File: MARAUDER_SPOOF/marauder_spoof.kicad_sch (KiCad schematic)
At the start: 26 parts, among them J2 Conn_01x10_Socket, J2 GPS, J3 Coil, J3 Conn_01x08_Socket, J4 Conn_01x08_Socket, J5 Conn_01x10_Socket, P1 USB_C_Plug_USB2.0, Q1 DMP2004TK-7, Q2 DMP2004TK-7, SW7 RESET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

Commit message: update layout magspoof-wifi
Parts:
- removed F1: 0.5A, Fuse:Fuse_0805_2012Metric, symbol Device:Fuse_Small
- removed J4: Conn_01x08_Socket, Connector_PinHeader_2.54mm:PinHeader_1x08_P2.54mm_Vertical, symbol Connector:Conn_01x08_Socket
- removed J5: Conn_01x10_Socket, Connector_PinHeader_2.54mm:PinHeader_1x10_P2.54mm_Vertical, symbol Connector:Conn_01x10_Socket
- removed Q1, Q2: DMP2004TK-7, Package_TO_SOT_THT:TO-92_Inline, symbol Transistor_FET:BS250
- added C4: 10uF, Capacitor_SMD:C_0603_1608Metric, symbol Device:C_Small
- added Q1, Q2: DMP2004TK-7, Package_TO_SOT_SMD:SOT-23, symbol Device:Q_NMOS_GSD
- J2: footprint Connector_PinHeader_2.54mm:PinHeader_1x10_P2.54mm_Horizontal -> Connector_PinHeader_2.54mm:PinHeader_1x10_P2.54mm_Vertical
- J3: footprint Connector_PinHeader_2.54mm:PinHeader_1x08_P2.54mm_Horizontal -> Connector_PinHeader_2.54mm:PinHeader_1x08_P2.54mm_Vertical
- R5, R6, R7, R8, R9: footprint (none) -> Resistor_SMD:R_0603_1608Metric
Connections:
- net +3V3: now also C4.1
- net GND: now also C4.2
- net at R8.1: now also Q1.2 (S)
- net at R6.1, R7.2: now also Q1.1 (G), Q2.1 (G)
- net at R6.2: now also Q1.3 (D), Q2.3 (D)
- net at R9.1: now also Q2.2 (S)
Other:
- moved on the sheet: C4

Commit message: Add_resistors_BOM_
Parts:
- P1: LCSC# C2987386 -> C2760486
- Q1, Q2: manf# (none) -> DMP2004TK-7; provedor (none) -> MOUSER
- R5, R6: LCSC# (none) -> C217281; manf# (none) -> CR-03JL7---10K; provedor (none) -> LCSC
- R7: LCSC# (none) -> C2692872; provedor (none) -> LCSC
- R8, R9: LCSC# (none) -> C394547; provedor (none) -> LCSC
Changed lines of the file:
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@@
+      (effects (font (size 1.27 1.27)) hide)
+    )
+    (property "LCSC#" "C394547" (at 202.184 139.446 0)
+      (effects (font (size 1.27 1.27)) hide)
+    )
+    (property "provedor" "LCSC" (at 202.184 139.446 0)
       (effects (font (size 1.27 1.27)) hide)
     )
@@
       (effects (font (size 1.27 1.27)) hide)
     )
+    (property "manf#" "DMP2004TK-7" (at 212.344 129.54 0)
+      (effects (font (size 1.27 1.27)) hide)
+    )
+    (property "provedor" "MOUSER" (at 212.344 129.54 0)
+      (effects (font (size 1.27 1.27)) hide)
+    )
     (pin "1")
     (pin "2")
@@
     )
     (property "Datasheet" "~" (at 191.008 113.919 0)
+      (effects (font (size 1.27 1.27)) hide)
+    )
+    (property "LCSC#" "C217281" (at 191.008 113.919 0)
+      (effects (font (size 1.27 1.27)) hide)
+    )
+    (property "manf#" "CR-03JL7---10K" (at 191.008 113.919 0)
+      (effects (font (size 1.27 1.27)) hide)
+    )
+    (property "provedor" "LCSC" (at 191.008 113.919 0)
       (effects (font (size 1.27 1.27)) hide)
     )
@@
       (effects (font (size 1.27 1.27)) hide)
     )
-    (property "LCSC#" "C2987386" (at 113.284 133.731 0)
+    (property "LCSC#" "C2760486" (at 113.284 133.731 0)
       (effects (font (size 1.27 1.27)) hide)
     )
@@
       (effects (font (size 1.27 1.27)) hide)
     )
+    (property "LCSC#" "C2692872" (at 181.356 120.269 0)
+      (effects (font (size 1.27 1.27)) hide)
+    )
+    (property "provedor" "LCSC" (at 181.356 120.269 0)
+      (effects (font (size 1.27 1.27)) hide)
+    )
     (pin "1")
     (pin "2")
@@
       (effects (font (size 1.27 1.27)) hide)
     )
+    (property "LCSC#" "C394547" (at 214.884 139.446 0)
+      (effects (font (size 1.27 1.27)) hide)
+    )
+    (property "provedor" "LCSC" (at 214.884 139.446 0)
+      (effects (font (size 1.27 1.27)) hide)
+    )
     (pin "1")
     (pin "2")
@@
       (effects (font (size 1.27 1.27)) hide)
     )
+    (property "manf#" "DMP2004TK-7" (at 199.644 120.269 0)
+      (effects (font (size 1.27 1.27)) hide)
+    )
+    (property "provedor" "MOUSER" (at 199.644 120.269 0)
+      (effects (font (size 1.27 1.27)) hide)
+    )
     (pin "1")
     (pin "2")
@@
       (effects (font (size 1.27 1.27)) hide)
     )
+    (property "LCSC#" "C217281" (at 177.038 52.324 0)
+      (effects (font (size 1.27 1.27)) hide)
+    )
+    (property "manf#" "CR-03JL7---10K" (at 177.038 52.324 0)
+      (effects (font (size 1.27 1.27)) hide)
+    )
+    (property "provedor" "LCSC" (at 177.038 52.324 0)
+      (effects (font (size 1.27 1.27)) hide)
+    )

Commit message: Add_subg_BOM
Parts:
- Q1, Q2: footprint Package_TO_SOT_SMD:SOT-23 -> Package_TO_SOT_SMD:SOT-523
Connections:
- no-connect marks 19 -> 29
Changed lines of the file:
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@@
   (junction (at 137.922 126.111) (diameter 0) (color 0 0 0 0)
   )
+  (no_connect (at 182.372 73.914))
   (no_connect (at 228.6 73.914))
   (no_connect (at 228.6 51.054))
   (no_connect (at 228.6 61.214))
+  (no_connect (at 182.245 43.434))
+  (no_connect (at 182.245 48.514))
   (no_connect (at 228.6 81.534))
+  (no_connect (at 233.68 86.614))
   (no_connect (at 53.213 37.973))
   (no_connect (at 228.6 63.754))
@@
   (no_connect (at 187.96 51.054))
   (no_connect (at 228.6 53.594))
+  (no_connect (at 182.245 81.534))
   (no_connect (at 228.6 78.994))
   (no_connect (at 27.813 37.973))
+  (no_connect (at 231.648 84.074))
   (no_connect (at 228.6 58.674))
   (no_connect (at 187.96 56.134))
+  (no_connect (at 182.245 76.454))
   (no_connect (at 228.6 76.454))
   (no_connect (at 228.6 68.834))
+  (no_connect (at 182.245 45.974))
   (no_connect (at 187.96 53.594))
   (no_connect (at 228.6 56.134))
+  (no_connect (at 182.245 84.074))
+  (no_connect (at 182.245 78.994))
   (polyline (pts (xy 13.4112 97.4344) (xy 285.5722 97.4344))
     (stroke (width 0) (type default))
@@
   )
   (wire (pts (xy 177.038 61.214) (xy 187.96 61.214))
-    (stroke (width 0) (type default))
-  )
-  (polyline (pts (xy 208.28 90.17) (xy 208.28 89.916))
     (stroke (width 0) (type default))
   )
@@
       (effects (font (size 1.27 1.27)) (justify left))
     )
-    (property "Footprint" "Package_TO_SOT_SMD:SOT-23" (at 217.424 127 0)
+    (property "Footprint" "Package_TO_SOT_SMD:SOT-523" (at 217.424 127 0)
       (effects (font (size 1.27 1.27)) hide)
     )
@@
       (effects (font (size 1.27 1.27)) (justify left))
     )
-    (property "Footprint" "Package_TO_SOT_SMD:SOT-23" (at 204.724 117.729 0)
-      (effects (font (size 1.27 1.27)) hide)
-    )
+    (property "Footprint" "Package_TO_SOT_SMD:SOT-523" (at 204.724 117.729 0)
+      (effects (font (size 1.27 1.27)) hide)
+    )

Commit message: Update_BOM
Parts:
- J2: manf# PZ254R-11-10P -> (none)
- J3: manf# WMRR138F-0 -> WR301025-19M8-G
- J3: manf# PZ254-1-08-W-8.5 -> (none)
- P1: manf# TYPE-C-31-M-31 -> (none)
- R10, R11: manf# ERJ3RBD5101V -> (none)
- R12, R5, R6: manf# CR-03JL7---10K -> (none)
- U3: manf# TC4424AVOA713 -> (none)
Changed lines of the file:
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@@
       (effects (font (size 1.27 1.27)) hide)
     )
-    (property "manf#" "CR-03JL7---10K" (at 191.008 113.919 0)
+    (property "manf#" "" (at 191.008 113.919 0)
       (effects (font (size 1.27 1.27)) hide)
     )
@@
       (effects (font (size 1.27 1.27)) hide)
     )
-    (property "manf#" "CR-03JL7---10K" (at 56.261 136.398 0)
+    (property "manf#" "" (at 56.261 136.398 0)
       (effects (font (size 1.27 1.27)) hide)
     )
@@
       (effects (font (size 1.27 1.27)) hide)
     )
-    (property "manf#" "WMRR138F-0" (at -183.5658 139.1666 0)
+    (property "manf#" "WR301025-19M8-G" (at -183.5658 139.1666 0)
       (effects (font (size 1.27 1.27)) hide)
     )
@@
       (effects (font (size 1.27 1.27)) hide)
     )
-    (property "manf#" "PZ254-1-08-W-8.5" (at 116.713 36.068 0)
+    (property "manf#" "" (at 116.713 36.068 0)
       (effects (font (size 1.27 1.27)) hide)
     )
@@
       (effects (font (size 1.27 1.27)) hide)
     )
-    (property "manf#" "TYPE-C-31-M-31" (at 113.284 133.731 0)
+    (property "manf#" "" (at 113.284 133.731 0)
       (effects (font (size 1.27 1.27)) hide)
     )
@@
       (effects (font (size 1.27 1.27)) hide)
     )
-    (property "manf#" "ERJ3RBD5101V" (at 132.842 126.111 0)
+    (property "manf#" "" (at 132.842 126.111 0)
       (effects (font (size 1.27 1.27)) hide)
     )
@@
       (effects (font (size 1.27 1.27)) hide)
     )
-    (property "manf#" "ERJ3RBD5101V" (at 132.842 123.571 0)
+    (property "manf#" "" (at 132.842 123.571 0)
       (effects (font (size 1.27 1.27)) hide)
     )
@@
       (effects (font (size 1.27 1.27)) hide)
     )
-    (property "manf#" "CR-03JL7---10K" (at 55.118 116.967 0)
+    (property "manf#" "" (at 55.118 116.967 0)
       (effects (font (size 1.27 1.27)) hide)
     )
@@
       (effects (font (size 1.27 1.27)) hide)
     )
-    (property "manf#" "CR-03JL7---10K" (at 177.038 52.324 0)
+    (property "manf#" "" (at 177.038 52.324 0)
       (effects (font (size 1.27 1.27)) hide)
     )
@@
       (effects (font (size 1.27 1.27)) hide)
     )
-    (property "manf#" "PZ254R-11-10P" (at 117.602 73.2536 0)
+    (property "manf#" "" (at 117.602 73.2536 0)
       (effects (font (size 1.27 1.27)) hide)
     )
@@
       (effects (font (size 1.524 1.524)) hide)
     )
-    (property "manf#" "TC4424AVOA713" (at 40.513 44.323 0)
-      (effects (font (size 1.27 1.27)) hide)
-    )
+    (property "manf#" "" (at 40.513 44.323 0)
+      (effects (font (size 1.27 1.27)) hide)
+    )

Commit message: BOM updated
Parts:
- J2: now not fitted
- J2: LCSC# C492418 -> C57369
- J3: LCSC# C2894950 -> C492407
- R10, R11: LCSC# C191782 -> C156350
- R12, R5, R6: LCSC# C217281 -> C2930027
- SW7, SW8: LCSC# C2886897 -> (none); manf# (none) -> TL3342F450QG
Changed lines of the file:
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@@
       (effects (font (size 1.27 1.27)) hide)
     )
-    (property "manf#" "" (at 48.133 120.523 0)
-      (effects (font (size 1.27 1.27)) hide)
-    )
-    (property "LCSC#" "C2886897" (at 48.133 120.523 0)
+    (property "manf#" "TL3342F450QG" (at 48.133 120.523 0)
+      (effects (font (size 1.27 1.27)) hide)
+    )
+    (property "LCSC#" "" (at 48.133 120.523 0)
       (effects (font (size 1.27 1.27)) hide)
     )
@@
       (effects (font (size 1.27 1.27)) hide)
     )
-    (property "LCSC#" "C217281" (at 191.008 113.919 0)
+    (property "LCSC#" "C2930027" (at 191.008 113.919 0)
       (effects (font (size 1.27 1.27)) hide)
     )
@@
       (effects (font (size 1.27 1.27)) hide)
     )
-    (property "LCSC#" "C217281" (at 56.261 136.398 0)
+    (property "LCSC#" "C2930027" (at 56.261 136.398 0)
       (effects (font (size 1.27 1.27)) hide)
     )
@@
       (effects (font (size 1.27 1.27)) hide)
     )
-    (property "LCSC#" "C2894950" (at 116.713 36.068 0)
+    (property "LCSC#" "C492407" (at 116.713 36.068 0)
       (effects (font (size 1.27 1.27)) hide)
     )
@@
       (effects (font (size 1.27 1.27)) hide)
     )
-    (property "manf#" "" (at 49.657 141.605 0)
-      (effects (font (size 1.27 1.27)) hide)
-    )
-    (property "LCSC#" "C2886897" (at 49.657 141.605 0)
+    (property "manf#" "TL3342F450QG" (at 49.657 141.605 0)
+      (effects (font (size 1.27 1.27)) hide)
+    )
+    (property "LCSC#" "" (at 49.657 141.605 0)
       (effects (font (size 1.27 1.27)) hide)
     )
@@
   )
   (symbol (lib_id "Connector:Screw_Terminal_01x05") (at 275.209 124.587 0) (unit 1)
-    (in_bom yes) (on_board yes) (dnp no) (fields_autoplaced)
+    (in_bom yes) (on_board yes) (dnp yes) (fields_autoplaced)
     (property "Reference" "J2" (at 277.241 124.5869 0)
       (effects (font (size 1.27 1.27)) (justify left))
@@
       (effects (font (size 1.27 1.27)) hide)
     )
-    (property "LCSC#" "C191782" (at 132.842 126.111 0)
+    (property "LCSC#" "C156350" (at 132.842 126.111 0)
       (effects (font (size 1.27 1.27)) hide)
     )
@@
       (effects (font (size 1.27 1.27)) hide)
     )
-    (property "LCSC#" "C191782" (at 132.842 123.571 0)
+    (property "LCSC#" "C156350" (at 132.842 123.571 0)
       (effects (font (size 1.27 1.27)) hide)
     )
@@
       (effects (font (size 1.27 1.27)) hide)
     )
-    (property "LCSC#" "C217281" (at 55.118 116.967 0)
+    (property "LCSC#" "C2930027" (at 55.118 116.967 0)
       (effects (font (size 1.27 1.27)) hide)
     )
@@
       (effects (font (size 1.27 1.27)) hide)
     )
-    (property "LCSC#" "C217281" (at 177.038 52.324 0)
+    (property "LCSC#" "C2930027" (at 177.038 52.324 0)
       (effects (font (size 1.27 1.27)) hide)
     )
@@
       (effects (font (size 1.27 1.27)) hide)
     )
-    (property "LCSC#" "C492418" (at 117.602 73.2536 0)
-      (effects (font (size 1.27 1.27)) hide)
-    )
+    (property "LCSC#" "C57369" (at 117.602 73.2536 0)
+      (effects (font (size 1.27 1.27)) hide)
+    )

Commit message: MarauderSpoof's BOM updated
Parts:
- U1: value ESP32-S3-WROOM-1U-N16 -> ESP32-S3-WROOM-1U-N4; manf# ESP32-S3-WROOM-1U-N16 -> ESP32-S3-WROOM-1U-N4
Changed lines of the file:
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@@
       (effects (font (size 1.524 1.524)))
     )
-    (property "Value" "ESP32-S3-WROOM-1U-N16" (at 208.28 28.194 0)
+    (property "Value" "ESP32-S3-WROOM-1U-N4" (at 208.28 28.194 0)
       (effects (font (size 1.524 1.524)))
     )
@@
       (effects (font (size 1.524 1.524)) hide)
     )
-    (property "manf#" "ESP32-S3-WROOM-1U-N16" (at 187.96 35.814 0)
+    (property "manf#" "ESP32-S3-WROOM-1U-N4" (at 187.96 35.814 0)
       (effects (font (size 1.27 1.27)) hide)
     )

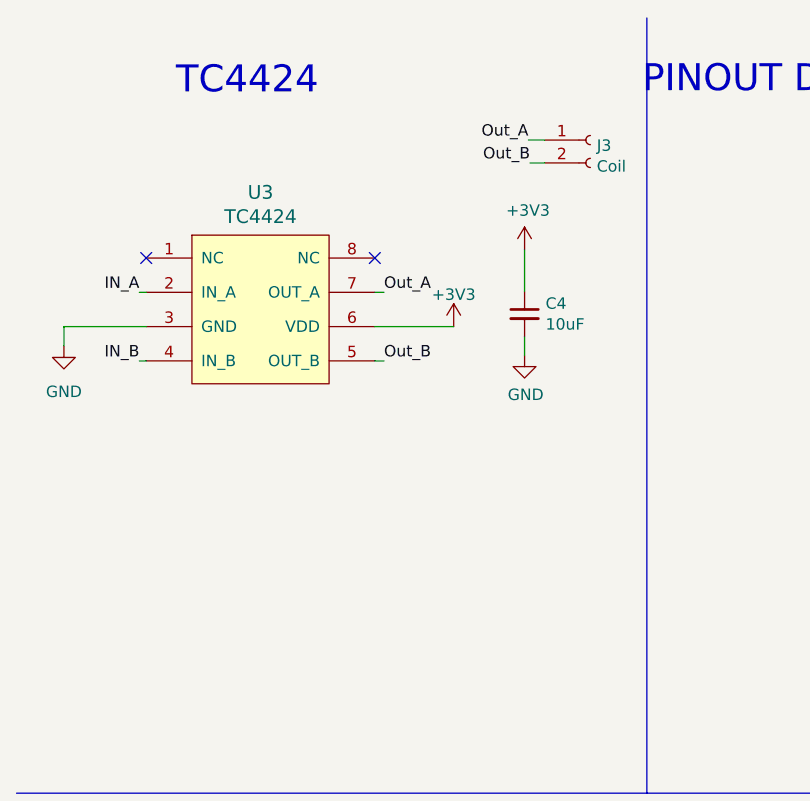
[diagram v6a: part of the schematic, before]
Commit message: feat(hw):Update coil
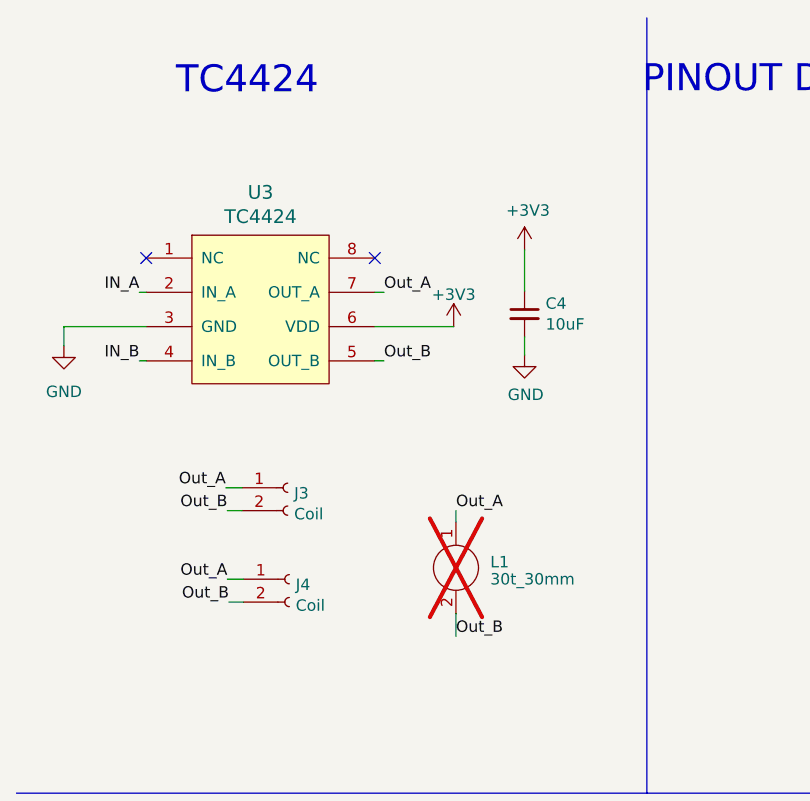
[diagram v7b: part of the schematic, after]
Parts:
- added J4: Coil, Connector_PinHeader_2.54mm:PinHeader_1x02_P2.54mm_Vertical, symbol Connector:Conn_01x02_Female
- added L1: 30t_30mm, Library:Coil_30t_30mm_0.2_0.2_0.6_0.3, symbol Magspoof:Coil_20t_35mm_0.2_0.6_0.3
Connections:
- net Out_A: now also J4.1 (Pin_1), L1.1
- net Out_B: now also J4.2 (Pin_2), L1.2
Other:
- moved on the sheet: J3

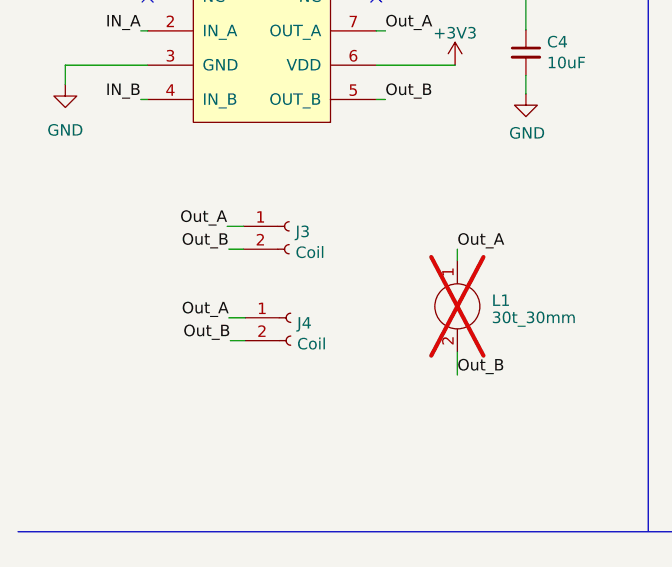
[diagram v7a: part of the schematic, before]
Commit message: fix(hw): add DNP for J1 and J4 and update SW1,2 and Q1,2 mfr.#
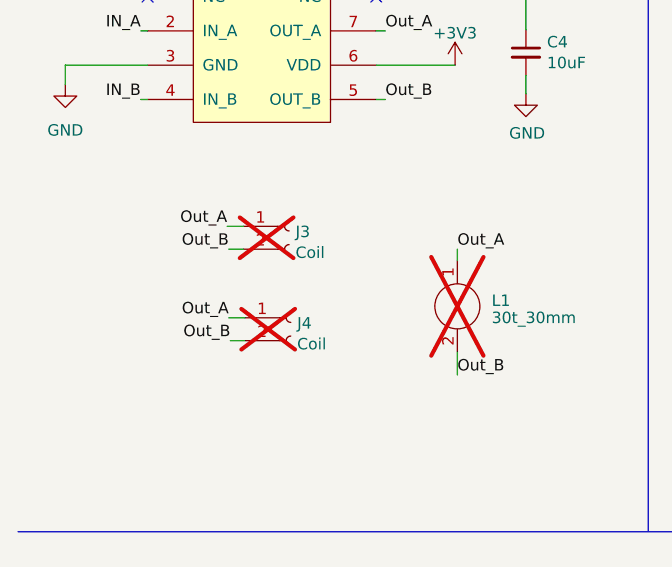
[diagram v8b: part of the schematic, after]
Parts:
- J3, J4: now not fitted
- Q1, Q2: LCSC# (none) -> C461051
- SW7: LCSC# (none) -> C318889
- SW8: LCSC# (none) -> C2886897
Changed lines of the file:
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@@
 			)
 		)
-		(property "LCSC#" ""
+		(property "LCSC#" "C318889 "
 			(at 48.133 120.523 0)
 			(effects
@@
 			)
 		)
+		(property "LCSC#" "C461051"
+			(at 212.344 129.54 0)
+			(effects
+				(font
+					(size 1.27 1.27)
+				)
+				(hide yes)
+			)
+		)
 		(pin "1"
 		)
@@
 		(in_bom yes)
 		(on_board yes)
-		(dnp no)
+		(dnp yes)
 		(property "Reference" "J3"
 			(at 44.2468 64.1096 0)
@@
 			)
 		)
-		(property "LCSC#" ""
+		(property "LCSC#" "C2886897"
 			(at 49.657 141.605 0)
 			(effects
@@
 			)
 		)
+		(property "LCSC#" "C461051"
+			(at 199.644 120.269 0)
+			(effects
+				(font
+					(size 1.27 1.27)
+				)
+				(hide yes)
+			)
+		)
 		(pin "1"
 		)
@@
 		(in_bom yes)
 		(on_board yes)
-		(dnp no)
+		(dnp yes)
 		(property "Reference" "J4"
 			(at 44.4246 74.2696 0)
